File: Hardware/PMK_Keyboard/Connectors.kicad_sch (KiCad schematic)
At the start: 4 parts, among them J101 USB4510-03-1-A, J102 Conn_01x02_MountingPin

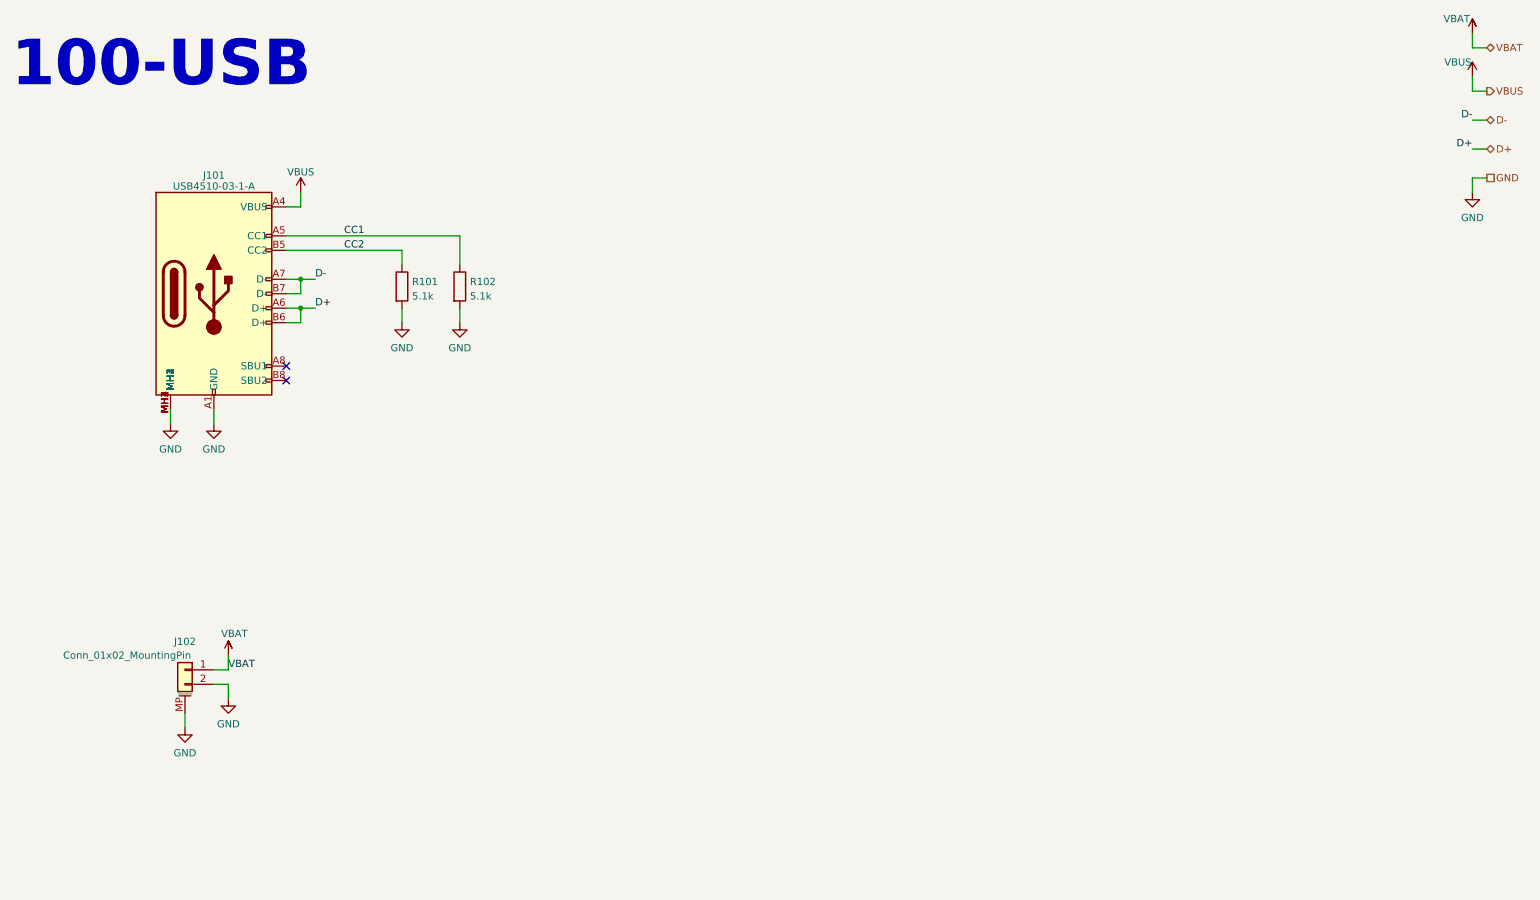
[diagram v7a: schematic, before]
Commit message: Added reverse polarity battery management
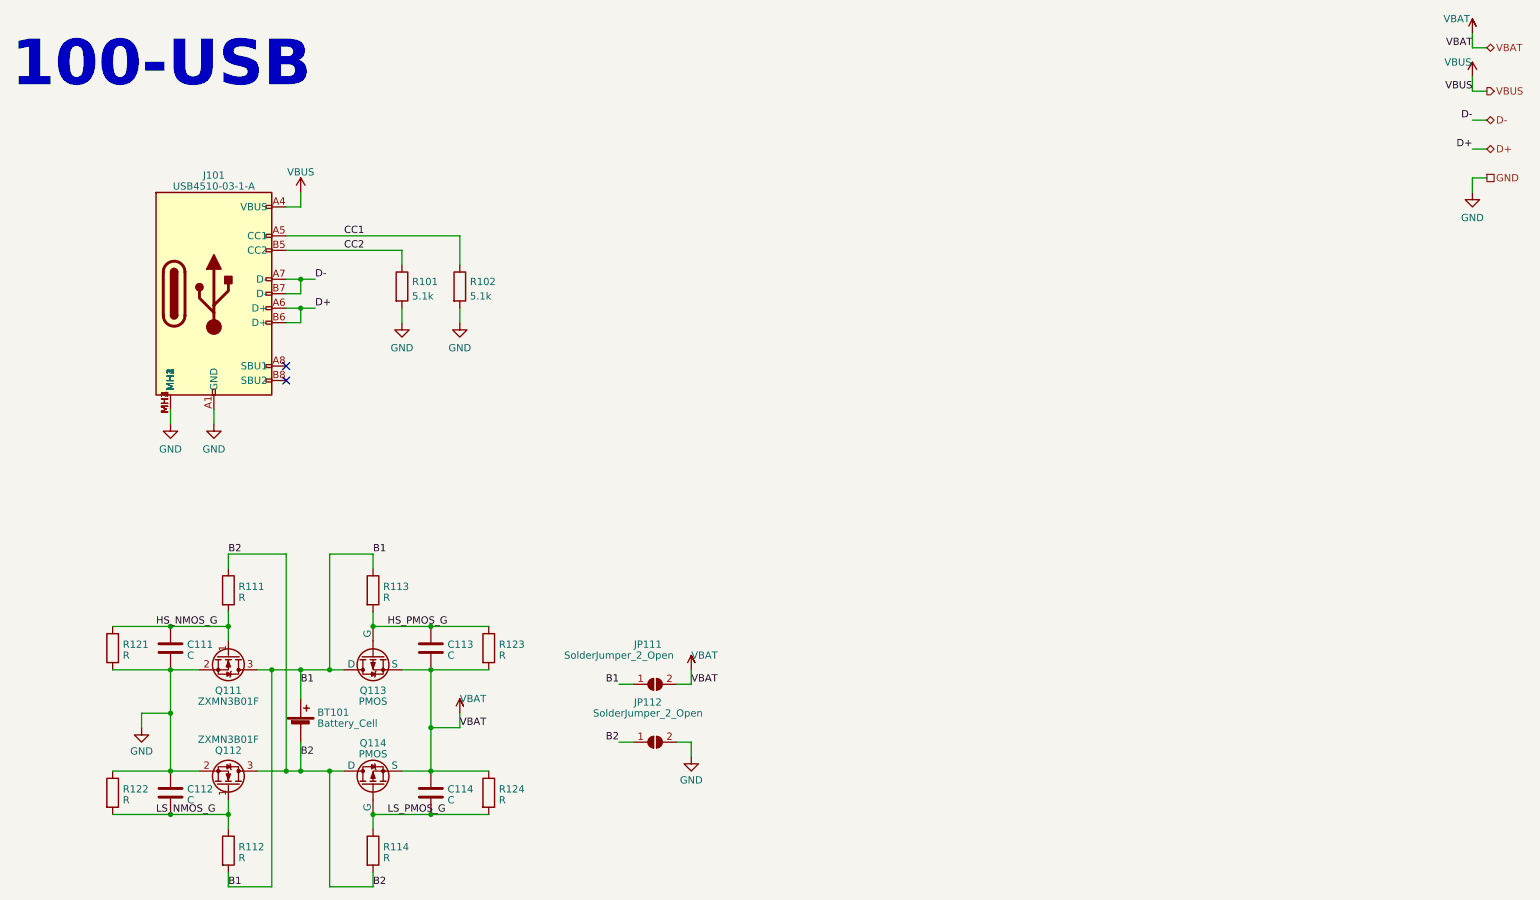
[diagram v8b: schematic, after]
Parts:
- removed J102: Conn_01x02_MountingPin, Component_lib:BatteryHolder_Keystone_1042_1x18650_DUALSIDE, symbol Connector_Generic_MountingPin:Conn_01x02_MountingPin
- added BT101: Battery_Cell, symbol Device:Battery_Cell
- added C111, C112, C113, C114: C, symbol Component_lib:C
- added JP111, JP112: SolderJumper_2_Open, symbol Jumper:SolderJumper_2_Open
- added Q111, Q112: ZXMN3B01F, Package_TO_SOT_SMD:SOT-23, symbol Component_lib:ZXMN3B01F
- added Q113, Q114: PMOS, symbol Simulation_SPICE:PMOS
- added R111, R112, R113, R114, R121, R122, R123, R124: R, symbol Component_lib:R
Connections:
- net GND: now also C111.2, C112.1, JP112.2 (B), Q111.2 (S), Q112.2 (S), R121.1, R122.1
- net VBAT: now also C113.2, C114.1, JP111.2 (B), Q113.3 (S), Q114.3 (S), R123.2, R124.1
- new net B1: BT101.1 (+), JP111.1 (A), Q111.3 (D), Q113.1 (D), R112.2, R113.1
- new net B2: BT101.2 (-), JP112.1 (A), Q112.3 (D), Q114.1 (D), R111.1, R114.2
- new net HS_NMOS_G: C111.1, Q111.1 (G), R111.2, R121.2
- new net HS_PMOS_G: C113.1, Q113.2 (G), R113.2, R123.1
- new net LS_NMOS_G: C112.2, Q112.1 (G), R112.1, R122.2
- new net LS_PMOS_G: C114.2, Q114.2 (G), R114.1, R124.2
